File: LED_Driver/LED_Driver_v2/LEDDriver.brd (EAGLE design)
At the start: 23.9 x 16.5 mm, 13 parts, among them Q1 DMP2012SN-7, U1 LM3409HV'LM3409HV'

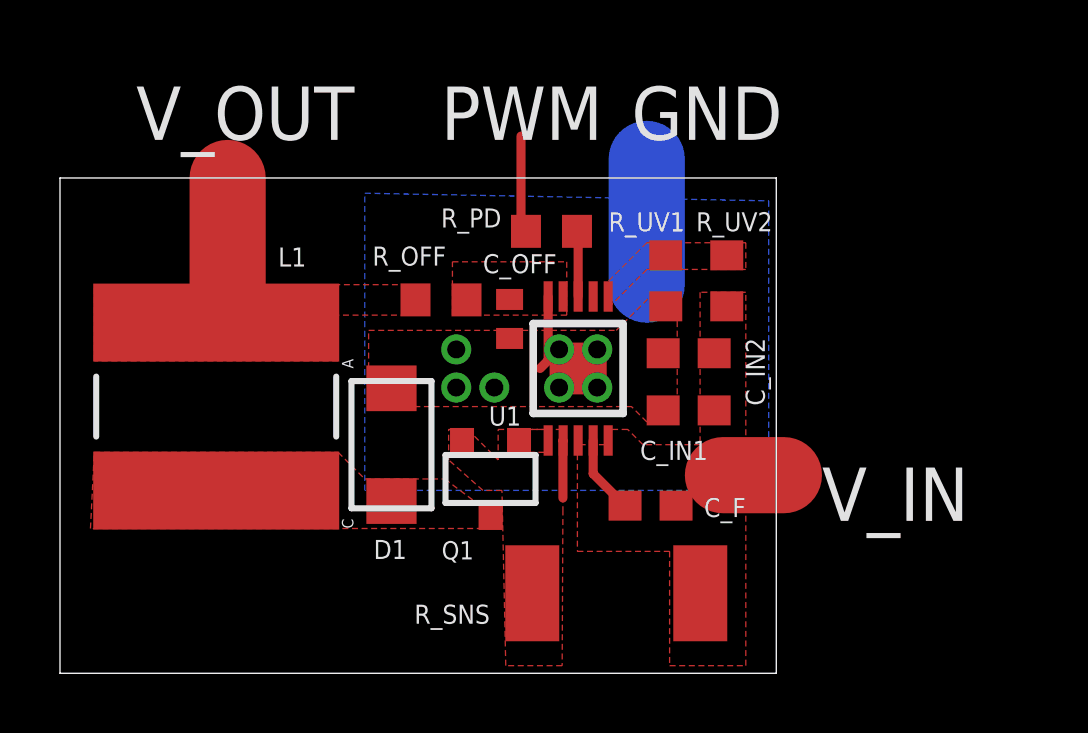
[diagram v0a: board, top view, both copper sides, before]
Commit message: Changes to traces and fills
Changed non-thermal fills to thermals/traces for most non-power
components. Main trace sizes used to route those components are 0.025"
and 0.012"
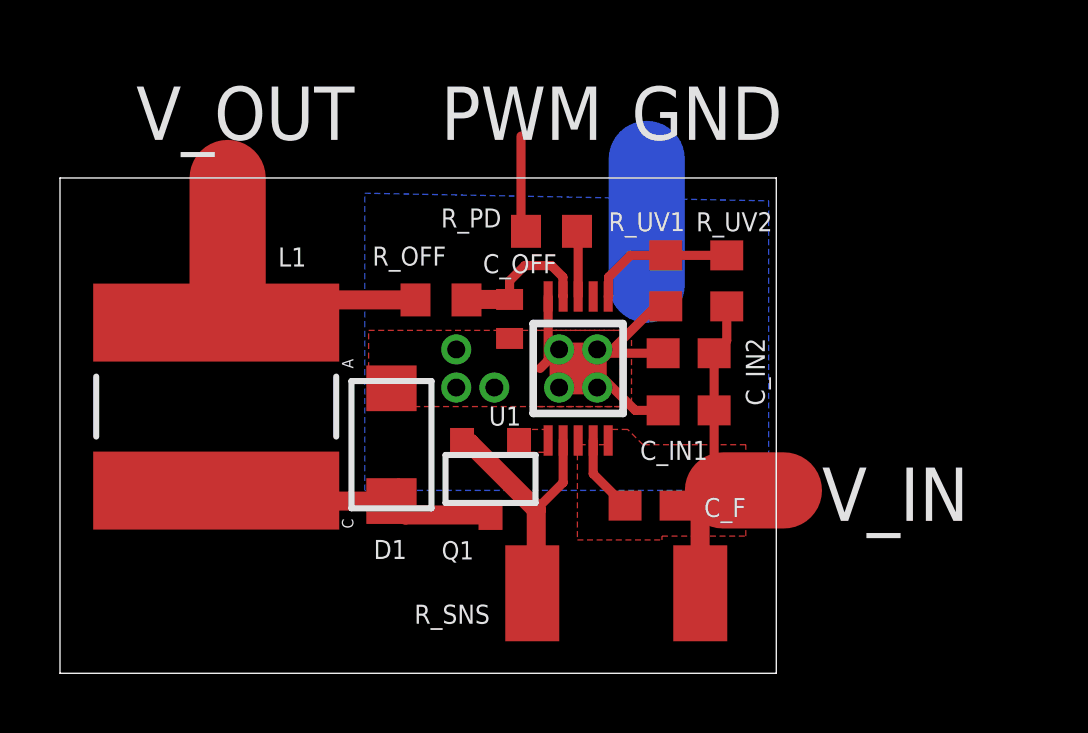
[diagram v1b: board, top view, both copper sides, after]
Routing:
- net V_IN: track 2.03 -> 12.3 mm
- net L1: track 0.65 -> 10.1 mm
- net GND: track 6.70 -> 15.3 mm
- net V_OUT: track 9.42 -> 16.8 mm
- net N$8: track 1.93 -> 8.91 mm
- net N$2: track 0.00 -> 4.89 mm
- net N$6: track 0.00 -> 4.86 mm
- removed copper zone on layer 1, net L1
- removed copper zone on layer 1, net N$2
- removed copper zone on layer 1, net N$6
- removed copper zone on layer 1, net N$8
- removed copper zone on layer 1, net V_OUT
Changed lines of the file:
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@@
 <vertex x="10.16" y="6.096"/>
 </polygon>
-<polygon width="0.3048" layer="1" thermals="no">
+<polygon width="0.3048" layer="1">
 <vertex x="10.287" y="11.43"/>
-<vertex x="18.542" y="11.43"/>
-<vertex x="19.812" y="12.7"/>
-<vertex x="20.574" y="12.7"/>
-<vertex x="20.574" y="8.382"/>
-<vertex x="19.558" y="8.382"/>
+<vertex x="19.05" y="11.43"/>
 <vertex x="19.05" y="8.89"/>
 <vertex x="10.287" y="8.89"/>
@@
 <via x="13.208" y="9.525" extent="1-16" drill="0.6"/>
 <via x="14.478" y="9.525" extent="1-16" drill="0.6"/>
+<wire x1="20.105" y1="12.143" x2="20.193" y2="12.231" width="0.4064" layer="1"/>
+<polygon width="0.254" layer="1" thermals="no">
+<vertex x="15.875" y="11.43"/>
+<vertex x="18.669" y="11.43"/>
+<vertex x="18.669" y="8.89"/>
+<vertex x="15.875" y="8.89"/>
+</polygon>
+<wire x1="20.193" y1="12.231" x2="19.851" y2="12.231" width="0.3048" layer="1"/>
+<wire x1="19.851" y1="12.231" x2="18.288" y2="10.668" width="0.3048" layer="1"/>
+<wire x1="17.78" y1="10.16" x2="17.272" y2="10.16" width="0.3048" layer="1"/>
+<wire x1="20.105" y1="10.668" x2="18.288" y2="10.668" width="0.3048" layer="1"/>
+<wire x1="18.288" y1="10.668" x2="17.78" y2="10.16" width="0.3048" layer="1"/>
+<wire x1="20.105" y1="8.763" x2="19.177" y2="8.763" width="0.3048" layer="1"/>
+<wire x1="19.177" y1="8.763" x2="17.78" y2="10.16" width="0.3048" layer="1"/>
 </signal>
 <signal name="V_IN">
@@
 <polygon width="0.254" layer="1" thermals="no">
 <vertex x="17.2466" y="7.62"/>
-<vertex x="17.2466" y="4.064"/>
-<vertex x="20.32" y="4.064"/>
-<vertex x="20.32" y="0.254"/>
-<vertex x="22.86" y="0.254"/>
-<vertex x="22.86" y="12.7"/>
-<vertex x="21.336" y="12.7"/>
-<vertex x="21.336" y="7.62"/>
+<vertex x="17.2466" y="4.445"/>
+<vertex x="20.066" y="4.445"/>
+<vertex x="20.066" y="4.572"/>
+<vertex x="22.86" y="4.572"/>
+<vertex x="22.86" y="7.62"/>
 <vertex x="19.431" y="7.62"/>
 <vertex x="18.923" y="8.128"/>
@@
 <vertex x="18.161" y="7.62"/>
 </polygon>
-<wire x1="22.098" y1="6.604" x2="24.13" y2="6.604" width="2.54" layer="1"/>
+<wire x1="22.098" y1="6.096" x2="24.13" y2="6.096" width="2.54" layer="1"/>
+<wire x1="21.805" y1="8.763" x2="21.844" y2="8.763" width="0.4064" layer="1"/>
+<wire x1="21.844" y1="6.858" x2="22.098" y2="6.858" width="0.4064" layer="1"/>
+<wire x1="22.098" y1="6.858" x2="22.098" y2="6.096" width="0.4064" layer="1"/>
+<wire x1="20.535" y1="5.588" x2="21.209" y2="5.588" width="0.635" layer="1"/>
+<wire x1="21.209" y1="5.588" x2="21.336" y2="5.461" width="0.635" layer="1"/>
+<wire x1="21.336" y1="5.461" x2="21.336" y2="2.673" width="0.635" layer="1"/>
+<wire x1="21.336" y1="2.673" x2="21.342" y2="2.667" width="0.635" layer="1"/>
+<wire x1="22.225" y1="12.231" x2="22.225" y2="11.088" width="0.3048" layer="1"/>
+<wire x1="22.225" y1="11.088" x2="21.805" y2="10.668" width="0.3048" layer="1"/>
+<wire x1="21.805" y1="10.668" x2="21.805" y2="8.763" width="0.3048" layer="1"/>
+<wire x1="21.805" y1="8.763" x2="21.805" y2="6.897" width="0.3048" layer="1"/>
+<wire x1="21.805" y1="6.897" x2="21.844" y2="6.858" width="0.3048" layer="1"/>
 </signal>
 <signal name="N$2">
@@
 <contactref element="R_UV2" pad="1"/>
 <contactref element="U1" pad="1"/>
-<polygon width="0.3048" layer="1" thermals="no">
-<vertex x="18.288" y="13.081"/>
-<vertex x="19.558" y="14.351"/>
-<vertex x="22.86" y="14.351"/>
-<vertex x="22.86" y="13.462"/>
-<vertex x="19.558" y="13.462"/>
-<vertex x="18.288" y="12.192"/>
-</polygon>
+<wire x1="22.225" y1="13.931" x2="20.193" y2="13.931" width="0.3048" layer="1"/>
+<wire x1="20.193" y1="13.931" x2="19.011" y2="13.931" width="0.3048" layer="1"/>
+<wire x1="19.011" y1="13.931" x2="18.288" y2="13.208" width="0.3048" layer="1"/>
+<wire x1="18.288" y1="13.208" x2="18.288" y2="12.575540625" width="0.3048" layer="1"/>
+<wire x1="18.288" y1="12.575540625" x2="18.272759375" y2="12.5603" width="0.3048" layer="1"/>
 </signal>
 <signal name="V_OUT">
 <contactref element="L1" pad="2"/>
 <contactref element="R_OFF" pad="1"/>
-<polygon width="0.254" layer="1" thermals="no">
-<vertex x="1.143" y="12.954"/>
-<vertex x="12.192" y="12.954"/>
-<vertex x="12.192" y="11.938"/>
-<vertex x="9.271" y="11.938"/>
-<vertex x="9.271" y="10.414"/>
-<vertex x="1.143" y="10.414"/>
-</polygon>
 <wire x1="5.588" y1="11.684" x2="5.588" y2="11.69" width="2.54" layer="1"/>
 <wire x1="5.588" y1="11.69" x2="5.588" y2="16.51" width="2.54" layer="1"/>
 <wire x1="5.588" y1="11.684" x2="5.207" y2="15.494" width="0.4064" layer="1"/>
-<wire x1="5.588" y1="11.69" x2="5.08" y2="11.69" width="0.4064" layer="1"/>
+<wire x1="5.588" y1="11.69" x2="5.207" y2="11.69" width="0.4064" layer="1"/>
+<wire x1="5.207" y1="11.69" x2="5.08" y2="11.69" width="0.4064" layer="1"/>
 <wire x1="5.08" y1="11.69" x2="5.08" y2="11.43" width="0.4064" layer="1"/>
+<wire x1="11.85" y1="12.446" x2="5.207" y2="12.446" width="0.635" layer="1"/>
+<wire x1="5.207" y1="12.446" x2="5.207" y2="11.69" width="0.635" layer="1"/>
 </signal>
 <signal name="N$6">
@@
 <contactref element="C_OFF" pad="1"/>
 <contactref element="U1" pad="4"/>
-<polygon width="0.254" layer="1" thermals="no">
-<vertex x="13.081" y="13.716"/>
-<vertex x="16.891" y="13.716"/>
-<vertex x="16.891" y="11.938"/>
-<vertex x="13.081" y="11.938"/>
-</polygon>
+<wire x1="14.986" y1="12.461" x2="13.565" y2="12.461" width="0.635" layer="1"/>
+<wire x1="13.565" y1="12.461" x2="13.55" y2="12.446" width="0.635" layer="1"/>
+<wire x1="14.986" y1="12.461" x2="14.986" y2="13.081" width="0.3048" layer="1"/>
+<wire x1="14.986" y1="13.081" x2="15.494" y2="13.589" width="0.3048" layer="1"/>
+<wire x1="15.494" y1="13.589" x2="16.383" y2="13.589" width="0.3048" layer="1"/>
+<wire x1="16.383" y1="13.589" x2="16.764" y2="13.208" width="0.3048" layer="1"/>
+<wire x1="16.764" y1="13.208" x2="16.764" y2="12.56791875" width="0.3048" layer="1"/>
+<wire x1="16.764" y1="12.56791875" x2="16.77161875" y2="12.5603" width="0.3048" layer="1"/>
 </signal>
 <signal name="PWM">
@@
 <contactref element="U1" pad="7"/>
 <contactref element="Q1" pad="3"/>
-<polygon width="0.3048" layer="1" thermals="no" rank="2">
-<vertex x="12.954" y="8.128"/>
-<vertex x="13.589" y="8.128"/>
-<vertex x="14.605" y="7.112"/>
-<vertex x="14.605" y="8.128"/>
-<vertex x="16.764" y="8.128"/>
-<vertex x="16.764" y="5.461"/>
-<vertex x="16.7386" y="0.254"/>
-<vertex x="14.859" y="0.254"/>
-<vertex x="14.732" y="6.096"/>
-<vertex x="14.097" y="6.096"/>
-<vertex x="12.954" y="7.112"/>
-</polygon>
-<wire x1="16.77161875" y1="7.7597" x2="16.764" y2="7.7597" width="0.3048" layer="1"/>
-<wire x1="16.764" y1="7.7597" x2="16.764" y2="5.842" width="0.3048" layer="1"/>
+<wire x1="13.401" y1="7.677" x2="13.659" y2="7.677" width="0.635" layer="1"/>
+<wire x1="13.659" y1="7.677" x2="15.875" y2="5.461" width="0.635" layer="1"/>
+<wire x1="15.875" y1="5.461" x2="15.875" y2="2.8" width="0.635" layer="1"/>
+<wire x1="15.875" y1="2.8" x2="15.742" y2="2.667" width="0.635" layer="1"/>
+<wire x1="16.77161875" y1="7.7597" x2="16.77161875" y2="6.35761875" width="0.3048" layer="1"/>
+<wire x1="16.77161875" y1="6.35761875" x2="15.875" y2="5.461" width="0.3048" layer="1"/>
 </signal>
 <signal name="N$1">
@@
 <contactref element="D1" pad="1"/>
 <wire x1="11.2776" y1="6.35" x2="11.049" y2="5.7404" width="0.3048" layer="1"/>
-<polygon width="0.3048" layer="1" thermals="no">
-<vertex x="1.143" y="7.366"/>
-<vertex x="9.271" y="7.366"/>
-<vertex x="10.16" y="6.477"/>
-<vertex x="12.827" y="6.477"/>
-<vertex x="13.843" y="5.715"/>
-<vertex x="14.732" y="5.715"/>
-<vertex x="14.732" y="4.826"/>
-<vertex x="1.016" y="4.826"/>
-</polygon>
+<wire x1="11.049" y1="5.7404" x2="5.5566" y2="5.7404" width="0.635" layer="1"/>
+<wire x1="5.5566" y1="5.7404" x2="5.207" y2="6.09" width="0.635" layer="1"/>
+<wire x1="14.351" y1="5.277" x2="11.5124" y2="5.277" width="0.635" layer="1"/>
+<wire x1="11.5124" y1="5.277" x2="11.049" y2="5.7404" width="0.635" layer="1"/>
 </signal>
 <signal name="N$4">
